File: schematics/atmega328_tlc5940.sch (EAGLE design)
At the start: 40 parts, among them IC2 74LS595N, IC3 74HC165N, IC4 74HC165N, U1 ATMEGA328P_PDIP, U2 TLC5940-NT, U3 TLC5940-NT, U4 TLC5940-NT

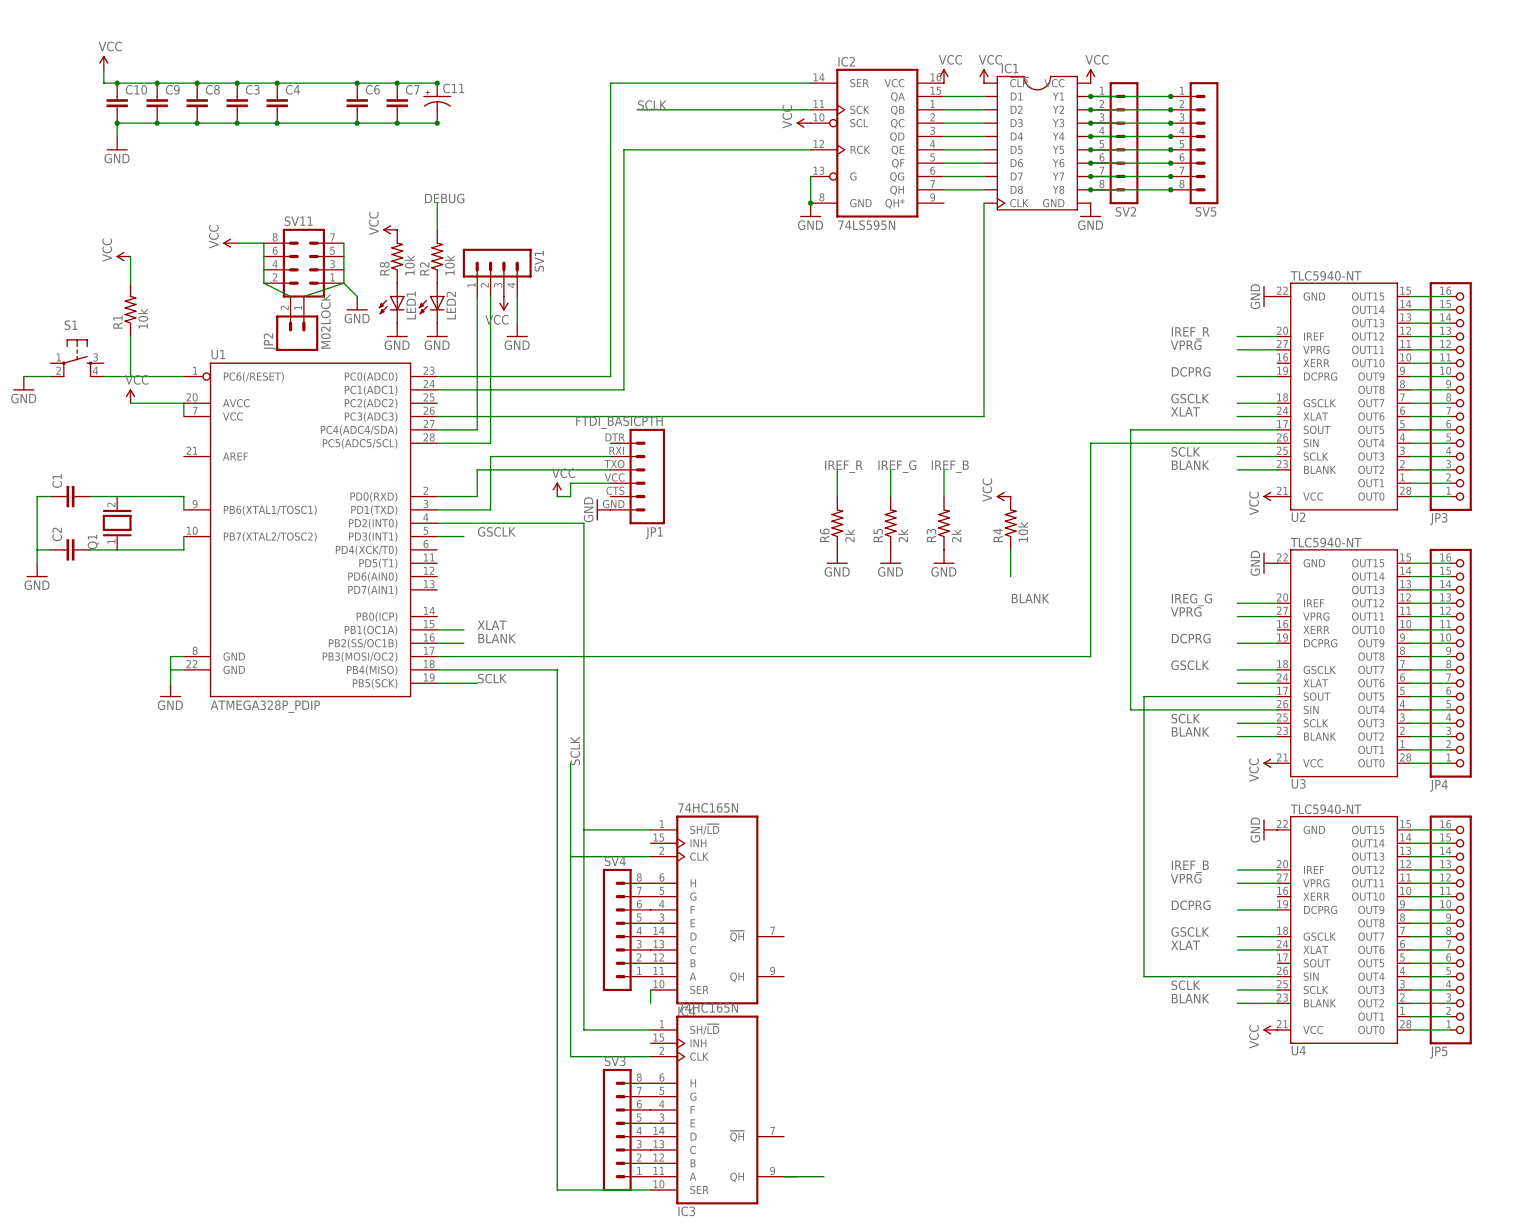
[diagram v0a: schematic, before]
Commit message: update schematic with row scanning mechanism and tlc5940 pinout changes.   clock is shared with all SR's
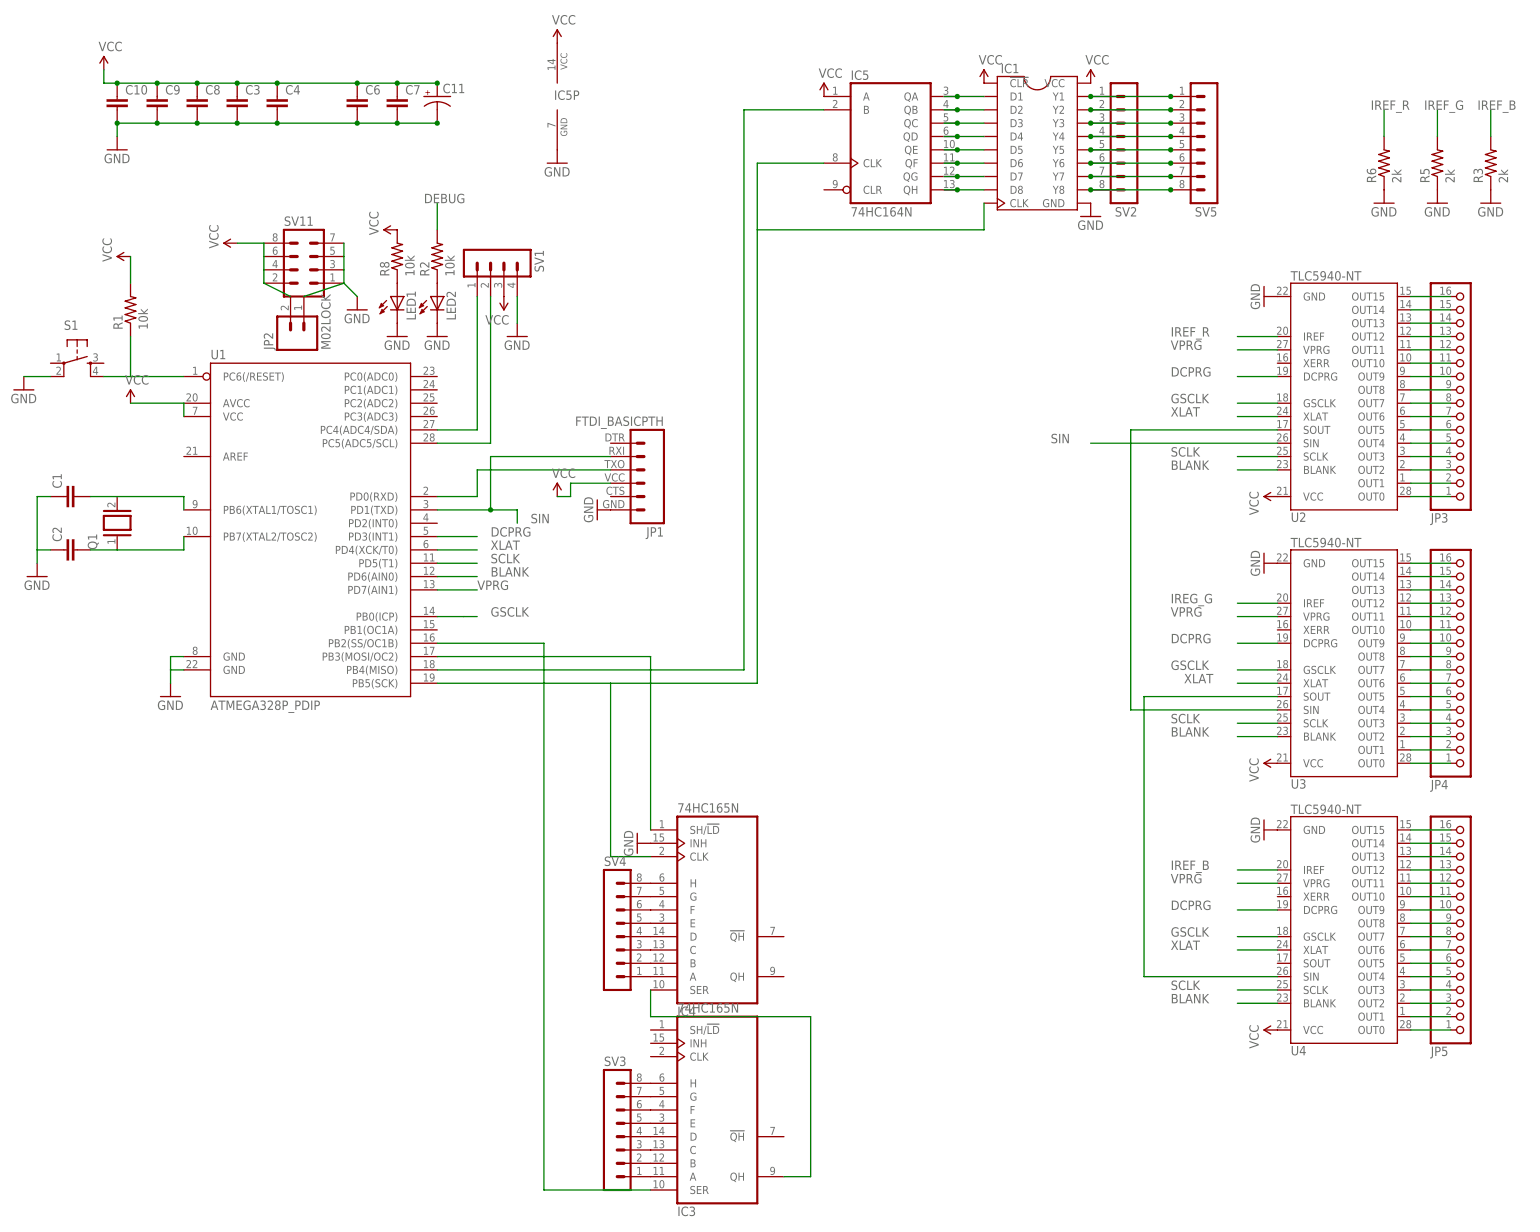
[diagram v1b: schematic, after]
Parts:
- removed IC2: 74LS595N, SparkFun-DigitalIC:74LS595N
- removed R4: 10k, SparkFun-Passives:RESISTORKIT
- added IC5: 74HC164N, 74xx-us:74HC164N
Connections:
- removed net N$105: U1.PB3(MOSI/OC2), U2.SIN
- removed net N$71: IC1.CLK, U1.PC3(ADC3)
- removed net N$96: IC3A.SER, U1.PB4(MISO)
- removed net N$98: IC4A.SER
- removed net N$99: IC3A.SH/!LD, IC4A.SH/!LD, U1.PD2(INT0)
- removed net TX$0: JP1.2, U1.PD1(TXD)
- new net N$61: IC4A.SH/!LD, U1.PB3(MOSI/OC2)
- new net N$70: IC3A.SER, U1.PB2(SS/OC1B)
- new net SIN: JP1.2, U1.PD1(TXD), U2.SIN
- net BLANK: now also U1.PD6(AIN0); no longer R4.1, U1.PB2(SS/OC1B)
- net DCPRG: now also U1.PD3(INT1)
- net GND: now also IC4A.INH, IC5P.GND; no longer IC2.G, IC2.GND
- net GSCLK: now also U1.PB0(ICP); no longer U1.PD3(INT1)
- net N$58: now also IC5A.QA; no longer IC2.QA
- net N$59: now also IC5A.B, U1.PB4(MISO); no longer IC3A.QH
- net N$60: now also IC1.CLK, IC4A.CLK, IC5A.CLK, U1.PB5(SCK); no longer IC2.RCK, U1.PC1(ADC1)
- net N$62: now also IC5A.QB; no longer IC2.QB
- net N$63: now also IC5A.QC; no longer IC2.QC
- net N$64: now also IC5A.QD; no longer IC2.QD
- net N$65: now also IC5A.QE; no longer IC2.QE
- net N$66: now also IC5A.QF; no longer IC2.QF
- net N$67: now also IC5A.QG; no longer IC2.QG
- net N$68: now also IC5A.QH; no longer IC2.QH
- net N$69: now also IC3A.QH, IC4A.SER; no longer IC2.SER, U1.PC0(ADC0)
- net SCLK: now also U1.PD5(T1); no longer IC2.SCK, IC3A.CLK, IC4A.CLK, U1.PB5(SCK)
- net VCC: now also IC5A.A, IC5P.VCC; no longer IC2.SCL, IC2.VCC, R4.2
- net VPRG: now also U1.PD7(AIN1)
- net XLAT: now also U1.PD4(XCK/T0); no longer U1.PB1(OC1A)
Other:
- moved on the sheet: R3, R5, R6
